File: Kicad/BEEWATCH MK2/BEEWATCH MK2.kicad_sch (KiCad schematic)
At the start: 0 parts

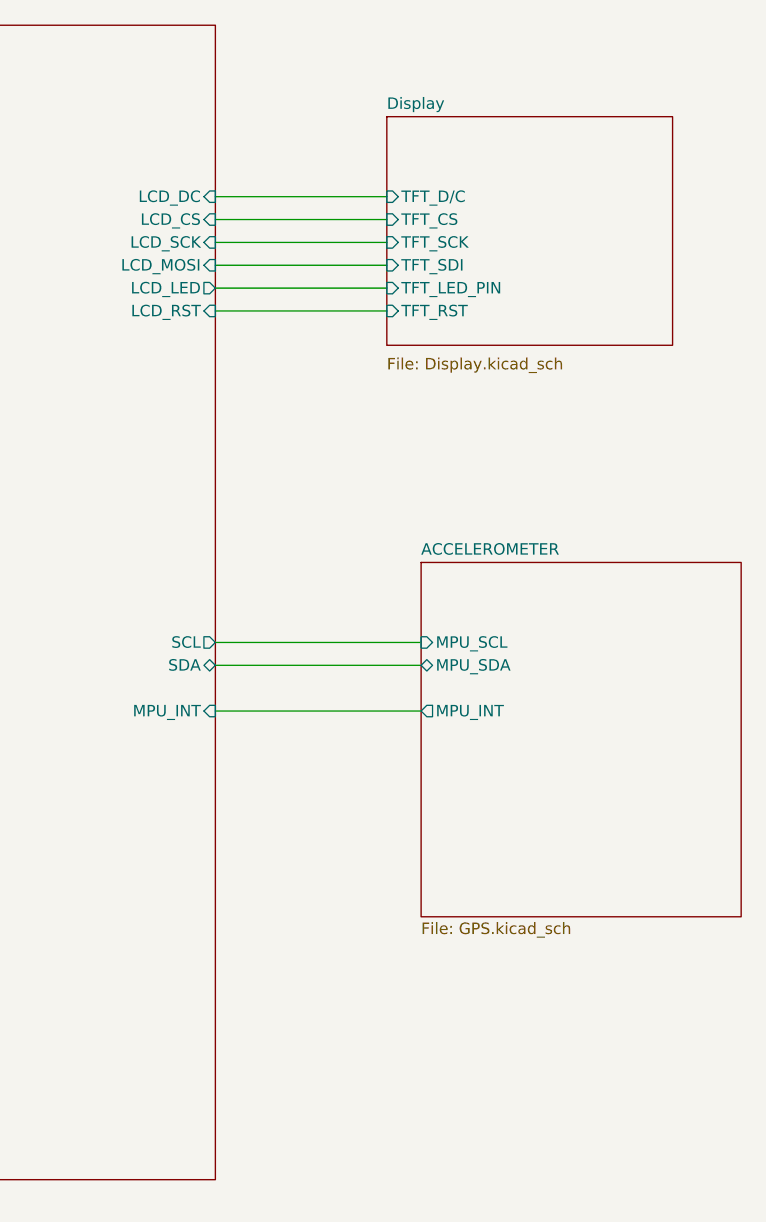
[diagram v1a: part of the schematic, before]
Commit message: Added display board schema
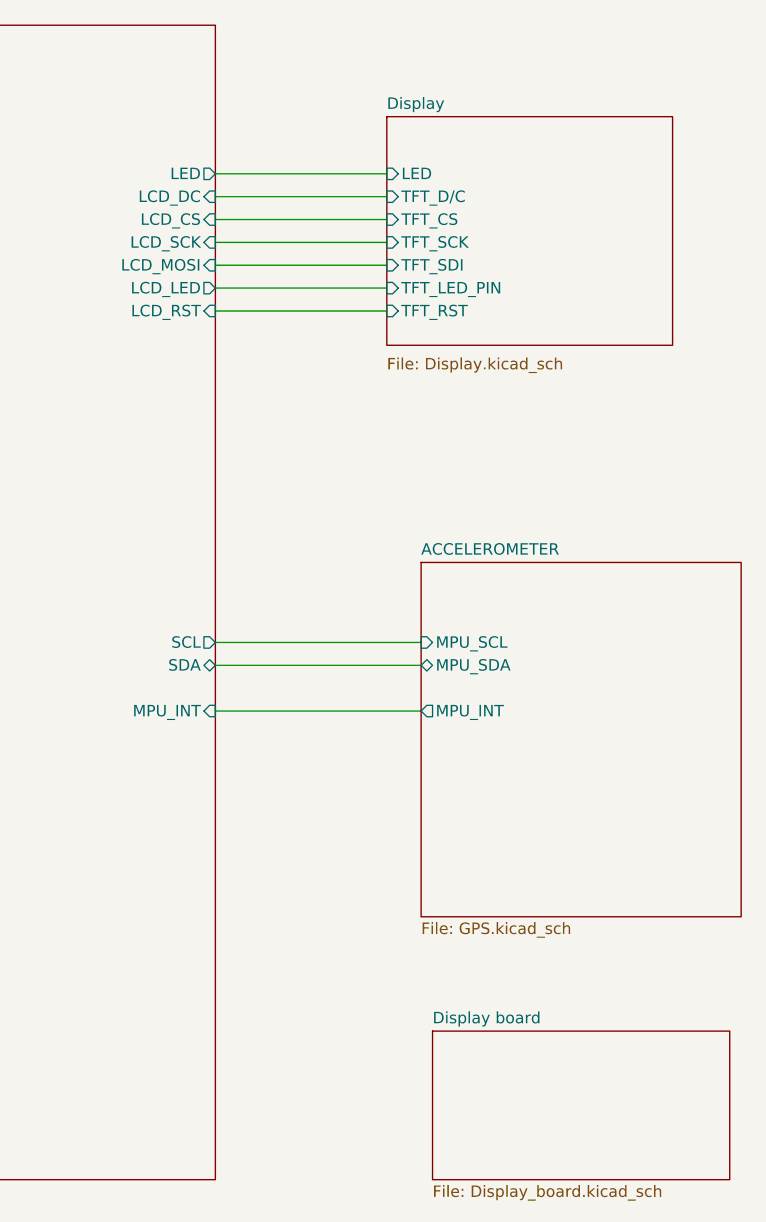
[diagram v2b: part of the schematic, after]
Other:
- added sheet Display board (Display_board.kicad_sch)
- sheet Display ports: added LED; removed none
- sheet ESP32 ports: added LED; removed none
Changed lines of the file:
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@@
+	(wire
+		(pts
+			(xy 184.15 44.45) (xy 203.2 44.45)
+		)
+		(stroke
+			(width 0)
+			(type default)
+		)
+	)
 	(wire
 		(pts
@@
 			(width 0)
 			(type default)
+		)
+	)
+	(sheet
+		(at 208.28 139.7)
+		(size 33.02 16.51)
+		(exclude_from_sim no)
+		(in_bom yes)
+		(on_board yes)
+		(dnp no)
+		(fields_autoplaced yes)
+		(stroke
+			(width 0.1524)
+			(type solid)
+		)
+		(fill
+			(color 0 0 0 0.0000)
+		)
+		(property "Sheetname" "Display board"
+			(at 208.28 138.9884 0)
+			(effects
+				(font
+					(size 1.27 1.27)
+				)
+				(justify left bottom)
+			)
+		)
+		(property "Sheetfile" "Display_board.kicad_sch"
+			(at 208.28 156.7946 0)
+			(effects
+				(font
+					(size 1.27 1.27)
+				)
+				(justify left top)
+			)
+		)
+		(instances
+			(project "BEEWATCH MK2"
+				(path "/e9c5fb53-480b-4989-8495-a3341ee99514"
+					(page "7")
+				)
+			)
 		)
 	)
@@
 			)
 		)
+		(pin "LED" input
+			(at 203.2 44.45 180)
+			(effects
+				(font
+					(size 1.27 1.27)
+				)
+				(justify left)
+			)
+		)
 		(instances
 			(project "BEEWATCH MK2"
@@
 			(project "BEEWATCH MK2"
 				(path "/e9c5fb53-480b-4989-8495-a3341ee99514"
-					(page "7")
+					(page "6")
 				)
 			)
@@
 			)
 		)
+		(pin "LED" output
+			(at 184.15 44.45 0)
+			(effects
+				(font
+					(size 1.27 1.27)
+				)
+				(justify right)
+			)
+		)
 		(instances
 			(project "BEEWATCH MK2"
@@
 			(project "BEEWATCH MK2"
 				(path "/e9c5fb53-480b-4989-8495-a3341ee99514"
-					(page "6")
-				)
-			)
+					(page "5")
+				)
+			)
